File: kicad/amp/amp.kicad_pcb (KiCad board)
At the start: 2 copper layers, 134 x 71 mm, 112 parts, among them J1 DC 12V IN, J2 IN L-G-R, J3 SPK L, J4 SPK R, Q1001 BC547, Q1002 BC547, Q1003 BC557, Q1004 BD139, Q1005 BD140, Q1006 BC547, Q2001 BC547, Q2002 BC547, Q2003 BC557, Q2004 BD139, Q2005 BD140, Q2006 BC547

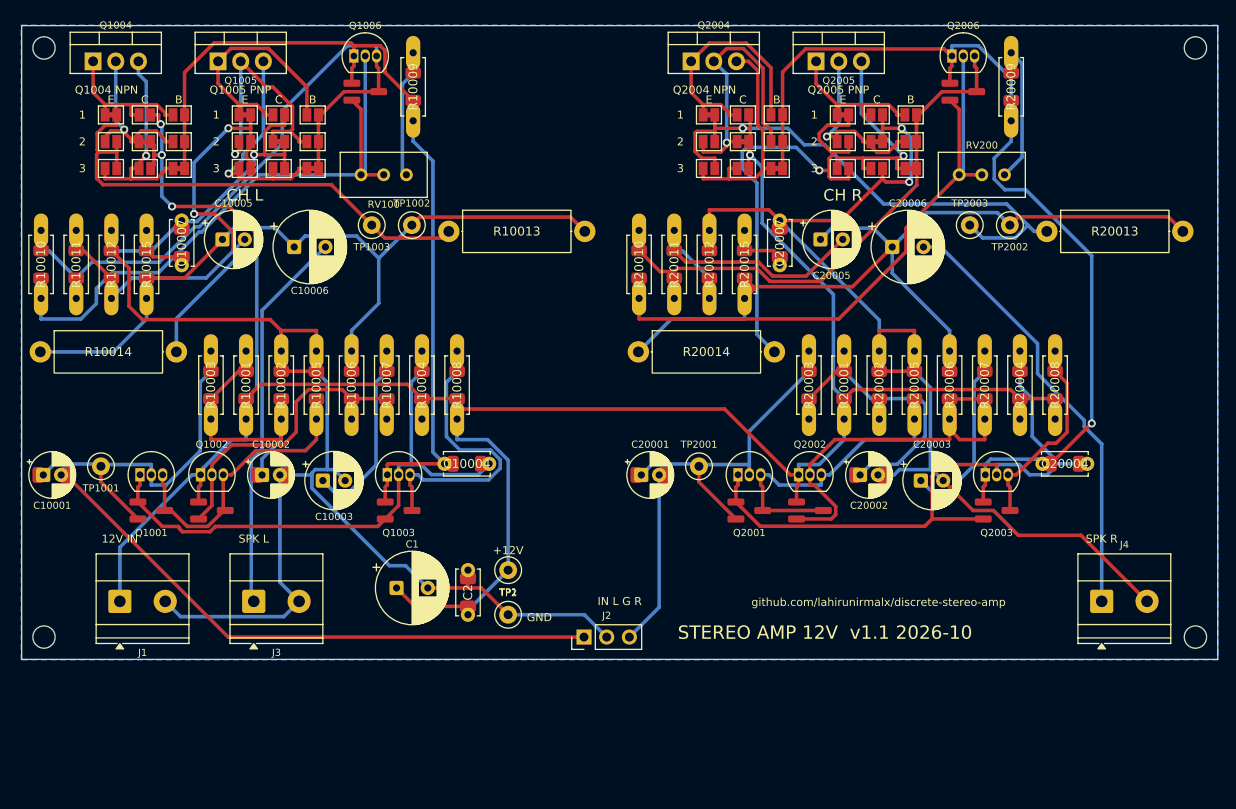
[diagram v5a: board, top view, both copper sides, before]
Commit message: Release 1.2: mirror-loaded front end, closed-loop PSU, VU tap, headphone board
- Amp: PNP input pair with NPN current-mirror load, LED-referenced current-source tail,
  NPN VAS with bootstrapped load from +12V, 220p Miller + 47p lead cap (THD 0.004% at 26 mW/8R,
  0.019% at 0.29 W; was 0.03 / 0.2). 1k VU meter tap per channel to header J5.
- PSU: BC547 error amplifier, 5.6 V zener fed from VOUT, 8.2k + 2k trimmer / 10k divider,
  2.2k drive, 47n/100n compensation. 12.0 V set point, 0.14 V dip on a 1 A step.
- New headphone board (DPDT switch, 120R series, DIRECT jumpers, 3.5 mm jack, panel-jack header).
- Boards: amp 134x85 / compact 100x98, PSU 90x58, hp 42x30; panel 155x155 with four boards.
  All 2-layer boards and the panel DRC clean; single-sided amp down to 15 errors.
- Toolchain: STAMP constant, reroute.sh second routing pass, rotated titles, link holes on
  jumper pads, 2 mm routing corridor per channel.
- Docs, BOMs, order guide, changelog, known issues rewritten for release 2.
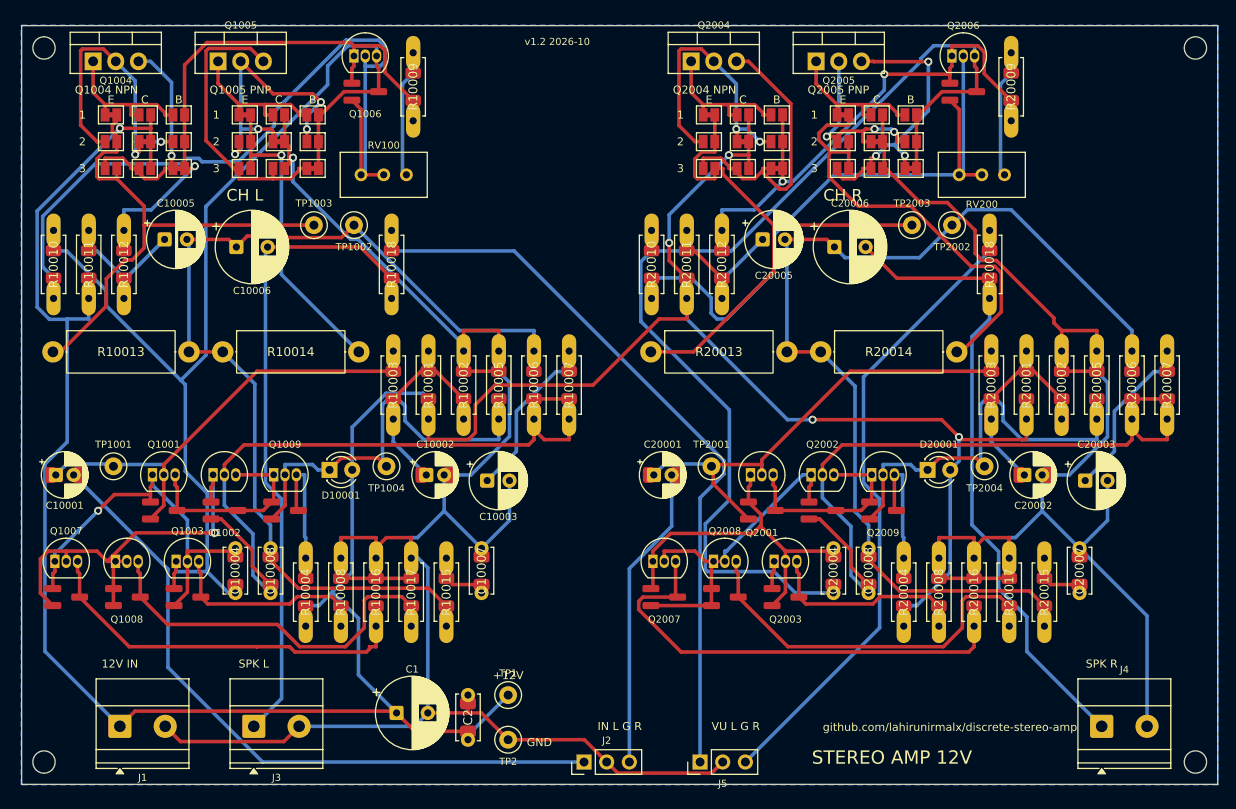
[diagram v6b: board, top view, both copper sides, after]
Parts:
- added C10008: 47p, Custom:C_P5_1206, F.Cu at (77.9, 113.6)
- added C20008: 47p, Custom:C_P5_1206, F.Cu at (144.9, 113.6)
- added D10001: LED red, LED_THT:LED_D3.0mm, F.Cu at (84.5, 99.8)
- added D20001: LED red, LED_THT:LED_D3.0mm, F.Cu at (151.5, 99.8)
- added J5: VU L-G-R, Connector_PinHeader_2.54mm:PinHeader_1x03_P2.54mm_Vertical, F.Cu at (126.0, 132.5)
- added Q1007: BC547, Custom:TO92_SOT23, F.Cu at (53.7, 110.0)
- added Q1008: BC547, Custom:TO92_SOT23, F.Cu at (60.5, 110.0)
- added Q1009: BC557, Custom:TO92_SOT23, F.Cu at (78.2, 100.3)
- added Q2007: BC547, Custom:TO92_SOT23, F.Cu at (120.7, 110.0)
- added Q2008: BC547, Custom:TO92_SOT23, F.Cu at (127.5, 110.0)
- added Q2009: BC557, Custom:TO92_SOT23, F.Cu at (145.2, 100.3)
- added R10016: 100, Custom:R_Axial_1206, F.Cu at (89.7, 117.3)
- added R10017: 100, Custom:R_Axial_1206, F.Cu at (93.6, 117.3)
- added R10018: 1k, Custom:R_Axial_1206, F.Cu at (91.4, 80.6)
- added R20016: 100, Custom:R_Axial_1206, F.Cu at (156.7, 117.3)
- added R20017: 100, Custom:R_Axial_1206, F.Cu at (160.6, 117.3)
- added R20018: 1k, Custom:R_Axial_1206, F.Cu at (158.4, 80.6)
- added TP1004: LED 10.2V, TestPoint:TestPoint_Loop_D2.50mm_Drill1.0mm, F.Cu at (90.9, 99.4)
- added TP2004: LED 10.2V, TestPoint:TestPoint_Loop_D2.50mm_Drill1.0mm, F.Cu at (157.9, 99.4)
- C10004, C20004: value 100p -> 220p
- Q1001, Q1002, Q2001, Q2002: value BC547 -> BC557
- Q1003, Q2003: value BC557 -> BC547
- R10004, R20004: value 4.7k -> 1.2k
- R10005, R20005: value 10k -> 4.7k
- TP1001, TP2001: value B1 5.9V -> B1 6.1V
- moved C20007 49.8 mm to (168.5, 113.6)
- moved R20015 49.8 mm to (164.6, 117.3)
- moved C10007 49.8 mm to (101.5, 113.6)
- moved R10015 49.8 mm to (97.6, 117.3)
- moved R20013 46.4 mm to (120.5, 86.5)
- moved R10013 46.4 mm to (53.5, 86.5)
- moved C10004 27.5 mm to (73.9, 113.6), turned to 90 degrees
- moved C20004 27.5 mm to (140.9, 113.6), turned to 90 degrees
- moved R10004 26.6 mm to (81.8, 117.3)
- moved R20004 26.6 mm to (148.8, 117.3)
- moved R20008 26.6 mm to (152.8, 117.3)
- moved R10008 26.6 mm to (85.8, 117.3)
- moved Q1003 25.6 mm to (67.3, 110.0)
- moved Q2003 25.6 mm to (134.3, 110.0)
- moved R10014 20.4 mm to (72.5, 86.5)
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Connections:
- C10004 pad 1: /VAS_L -> /B5_L
- C10004 pad 1S: /VAS_L -> /B5_L
- C10005 pad 1: /OUT_L -> Net-(C10005-Pad1)
- C10005 pad 2: Net-(C10005-Pad2) -> /OUT_L
- C20004 pad 1: /VAS_R -> /B5_R
- C20004 pad 1S: /VAS_R -> /B5_R
- C20005 pad 1: /OUT_R -> Net-(C20005-Pad1)
- C20005 pad 2: Net-(C20005-Pad2) -> /OUT_R
- Q1002 pad 1: +12V -> Net-(Q1002-C)
- Q1002 pad 1S: +12V -> Net-(Q1002-C)
- Q1003 pad 1: /VAS_L -> /B5_L
- Q1003 pad 1S: /VAS_L -> /B5_L
- Q2002 pad 1: +12V -> Net-(Q2002-C)
- Q2002 pad 1S: +12V -> Net-(Q2002-C)
- Q2003 pad 1: /VAS_R -> /B5_R
- Q2003 pad 1S: /VAS_R -> /B5_R
- R10004 pad 2: Net-(Q1001-C) -> Net-(Q1009-E)
- R10004 pad 2S: Net-(Q1001-C) -> Net-(Q1009-E)
- R10005 pad 1: Net-(Q1001-E) -> Net-(D10001-K)
- R10005 pad 1S: Net-(Q1001-E) -> Net-(D10001-K)
- R10008 pad 1: +12V -> Net-(Q1003-E)
- R10008 pad 1S: +12V -> Net-(Q1003-E)
- R10008 pad 2: Net-(Q1003-E) -> GND
- R10008 pad 2S: Net-(Q1003-E) -> GND
- R10011 pad 1: /B5_L -> +12V
- R10011 pad 1S: /B5_L -> +12V
- R10011 pad 2: Net-(C10005-Pad2) -> Net-(C10005-Pad1)
- R10011 pad 2S: Net-(C10005-Pad2) -> Net-(C10005-Pad1)
- R10012 pad 1: Net-(C10005-Pad2) -> Net-(C10005-Pad1)
- R10012 pad 1S: Net-(C10005-Pad2) -> Net-(C10005-Pad1)
- R10012 pad 2: GND -> /VAS_L
- R10012 pad 2S: GND -> /VAS_L
- R20004 pad 2: Net-(Q2001-C) -> Net-(Q2009-E)
- R20004 pad 2S: Net-(Q2001-C) -> Net-(Q2009-E)
- R20005 pad 1: Net-(Q2001-E) -> Net-(D20001-K)
- R20005 pad 1S: Net-(Q2001-E) -> Net-(D20001-K)
- R20008 pad 1: +12V -> Net-(Q2003-E)
- R20008 pad 1S: +12V -> Net-(Q2003-E)
- R20008 pad 2: Net-(Q2003-E) -> GND
- R20008 pad 2S: Net-(Q2003-E) -> GND
- R20011 pad 1: /B5_R -> +12V
- R20011 pad 1S: /B5_R -> +12V
- R20011 pad 2: Net-(C20005-Pad2) -> Net-(C20005-Pad1)
- R20011 pad 2S: Net-(C20005-Pad2) -> Net-(C20005-Pad1)
- R20012 pad 1: Net-(C20005-Pad2) -> Net-(C20005-Pad1)
- R20012 pad 1S: Net-(C20005-Pad2) -> Net-(C20005-Pad1)
- R20012 pad 2: GND -> /VAS_R
- R20012 pad 2S: GND -> /VAS_R
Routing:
- net /VU_L: track 0.00 -> 86.4 mm
- net /VU_R: track 0.00 -> 74.6 mm
- net +12V: track 274.7 -> 348.0 mm
- net /B5_R: track 63.3 -> 132.5 mm
- net Net-(Q2007-E): track 0.00 -> 53.9 mm
- net GND: track 305.2 -> 357.9 mm, vias 3 -> 1
- net /B5_L: track 80.9 -> 129.8 mm
- net /VAS_R: track 109.8 -> 62.1 mm, vias 1 -> 2
- net Net-(D10001-K): track 0.00 -> 47.1 mm
- net Net-(D20001-K): track 0.00 -> 47.1 mm
- net Net-(Q1002-C): track 0.00 -> 46.3 mm, vias 0 -> 1
- net Net-(Q1007-E): track 0.00 -> 44.8 mm
- net Net-(Q1008-E): track 0.00 -> 43.6 mm
- net Net-(Q2008-E): track 0.00 -> 43.6 mm
- net Net-(Q1002-B): track 36.8 -> 79.3 mm
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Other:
- board size 134 x 71 mm -> 134 x 85 mm
- board text added: "STEREO AMP 12V"
- board text added: "VU L G R"
- board text added: "v1.2 2026-10"
- board text removed: "STEREO AMP 12V v1.1 2026-10"
